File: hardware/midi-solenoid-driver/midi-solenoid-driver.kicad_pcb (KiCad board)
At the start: 2 copper layers, 113 x 62.7 mm, 80 parts, among them J1 LEFT_DATA, J2 Conn_02x03_Odd_Even, J3 RIGHT_DATA, J4 12V_IN, J5 SOLENOIDS_OUT_1, J6 SOLENOIDS_OUT_2, Q1 Q_NMOS_GDS, Q10 Q_NMOS_GDS, Q11 Q_NMOS_GDS, Q12 Q_NMOS_GDS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

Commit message: PCB mostly done.
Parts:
- added G***: LOGO, footprints:willemhillier.wordpress-logo, B.Cu at (321.0, 117.1)
- added REF**: MountingHole_4.3mm_M4, MountingHole:MountingHole_4.3mm_M4, F.Cu at (248.8, 80.8)
- added REF**: MountingHole_4.3mm_M4, MountingHole:MountingHole_4.3mm_M4, F.Cu at (352.8, 80.8)
- added REF**: MountingHole_4.3mm_M4, MountingHole:MountingHole_4.3mm_M4, F.Cu at (362.1, 143.8)
- added REF**: MountingHole_4.3mm_M4, MountingHole:MountingHole_4.3mm_M4, F.Cu at (239.6, 143.8)
- moved R2 8.46 mm to (334.7, 108.3), turned to 90 degrees
- moved RN3 3.30 mm to (324.2, 101.9)
- moved RN4 3.30 mm to (329.7, 101.9)
- moved R1 2.31 mm to (324.0, 105.5), turned to 0 degrees
- moved Q3 0.07 mm to (262.4, 128.9)
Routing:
- net /12V_FUSED2: track 82.5 -> 56.8 mm
- net +5V: track 95.3 -> 86.8 mm
- net Net-(J1-Pad4): track 109.3 -> 114.4 mm
- net /MIDI_CH_BIT2-3: track 22.2 -> 17.3 mm
- net Net-(RN3-Pad5): track 3.07 -> 6.62 mm
- net Net-(RN4-Pad2): track 6.06 -> 9.53 mm
- net Net-(RN3-Pad2): track 6.02 -> 9.32 mm
- net Net-(RN4-Pad5): track 2.91 -> 6.21 mm
- net /MIDI_CH_BIT0-1: track 20.7 -> 18.2 mm
- net /RESET: track 17.4 -> 19.4 mm
- net /MIDI_IN: track 3.96 -> 2.64 mm
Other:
- board size 113 x 62.7 mm -> 131.5 x 72 mm
- board text added: "+ -"
- board text added: "-+"
- board text added: "-+ -+ -+ -+ -+ -+ -+ -+ -+ -+ -+ -+ -+ -+ -+ -+"
- board text added: "1 <---- OUTPUTS ----> 16"
- board text added: "12V IN"
- board text added: "15A MAX"
- board text added: "16 15 14 13 12 11 10 9"
- board text added: "8 7 6 5 4 3 2 1"
- board text added: "BIT: 3 2 1 0"
- board text added: "BIT: 6 5 4 3 2 1 0 x"
- board text added: "CHANNEL SEL"
- board text added: "FUSE 1"
- board text added: "FUSE 2"
- board text added: "ICSP"
- board text added: "MIDI DATA"
- board text added: "MIDI PROGRAM"
- board text added: "MIDI Solenoid Driver Board"
- board text added: "More info on this board, including schematics, firmware, and board design files, are available at: https://github.com/willemcvu/midi-solenoid-driver"
- board text added: "NOTE RANGE SEL"
- board text added: "Willem Hillier rev1 19.209"

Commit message: USB interface schematic done
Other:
- rule pad_to_mask_clearance: 0.051 -> 0.04572
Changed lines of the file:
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@@
     (pad_size 1.524 1.524)
     (pad_drill 0.762)
-    (pad_to_mask_clearance 0.051)
+    (pad_to_mask_clearance 0.04572)
     (solder_mask_min_width 0.25)
     (aux_axis_origin 0 0)
@@
       (outputformat 1)
       (mirror false)
-      (drillshape 1)
+      (drillshape 0)
       (scaleselection 1)
-      (outputdirectory ""))
+      (outputdirectory "gerbers/"))
   )
   (net 0 "")

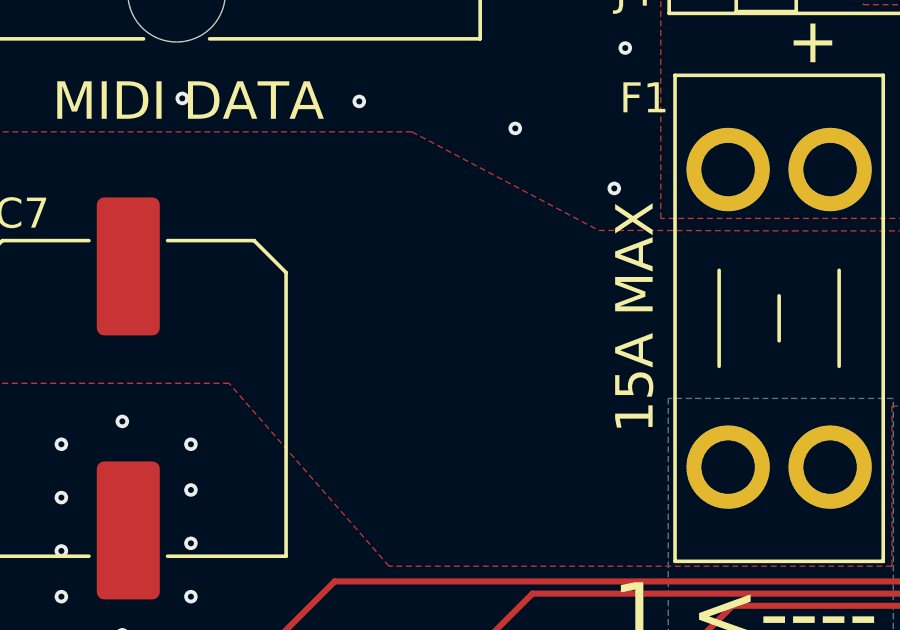
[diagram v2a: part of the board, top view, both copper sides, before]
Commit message: Added OSHW logo to driver board
 - Added logo
 - Made new gerbers
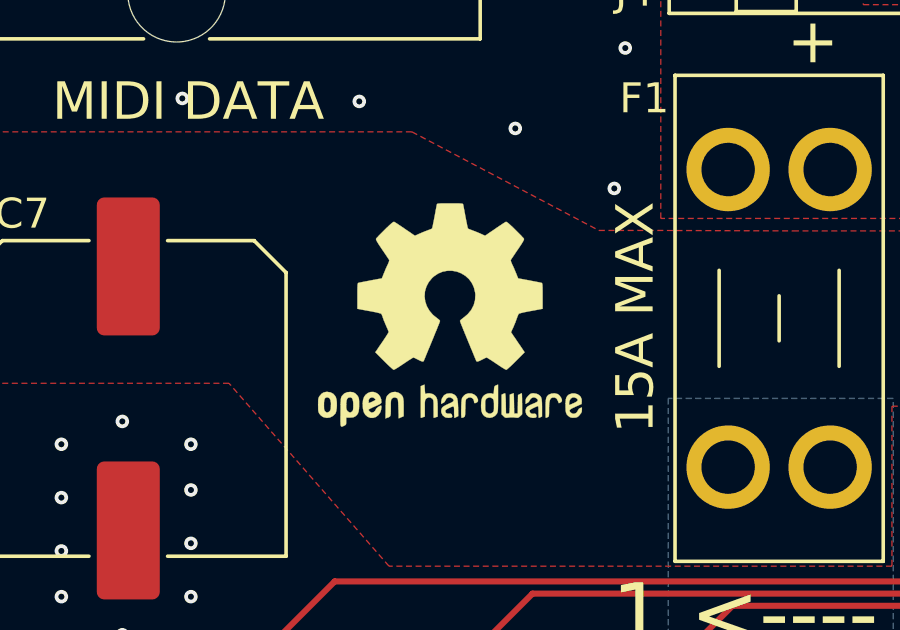
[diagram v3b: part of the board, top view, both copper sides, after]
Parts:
- added REF**: OSHW-Logo2_9.8x8mm_SilkScreen, Symbol:OSHW-Logo2_9.8x8mm_SilkScreen, B.Cu at (261.6, 108.9)
- added REF**: OSHW-Logo2_9.8x8mm_SilkScreen, Symbol:OSHW-Logo2_9.8x8mm_SilkScreen, F.Cu at (260.9, 109.0)
- moved G*** 0.36 mm to (321.0, 117.4)
